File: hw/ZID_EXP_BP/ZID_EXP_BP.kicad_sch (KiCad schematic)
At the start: 47 parts, among them J1 FFC/FPC-40 Socket, J2 Conn_02x05_2.54mm, J3 Conn_02x05_2.54mm, J4 USB-C PWR ONLY, J6 Conn_02x03_Odd_Even, J7 Conn_02x03_Odd_Even, J9 HDR 2x10 Pin, Q1 DMG2305UX, U1 74HCT138

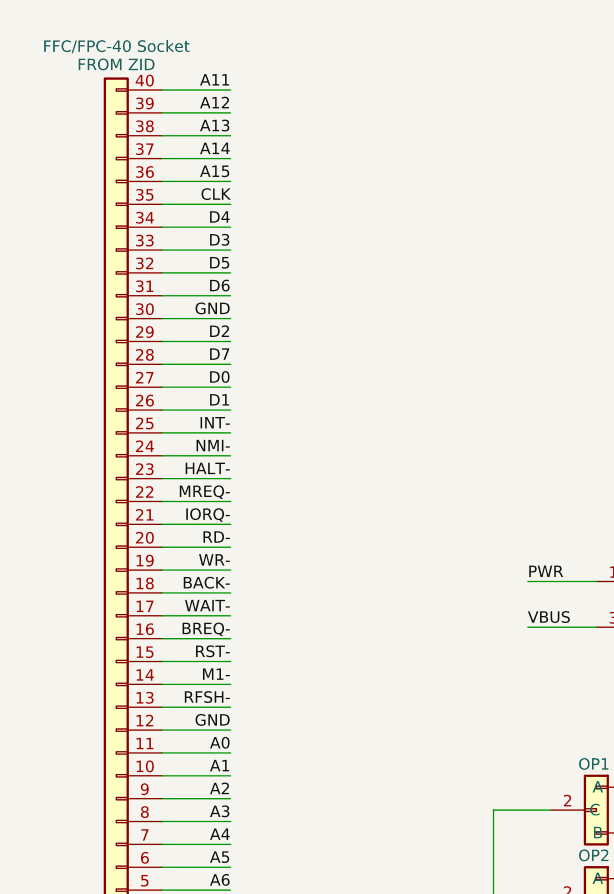
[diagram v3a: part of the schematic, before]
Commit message: 74FCT541 to 74FCT2245. Move GND around CLK on ZID-POD connector
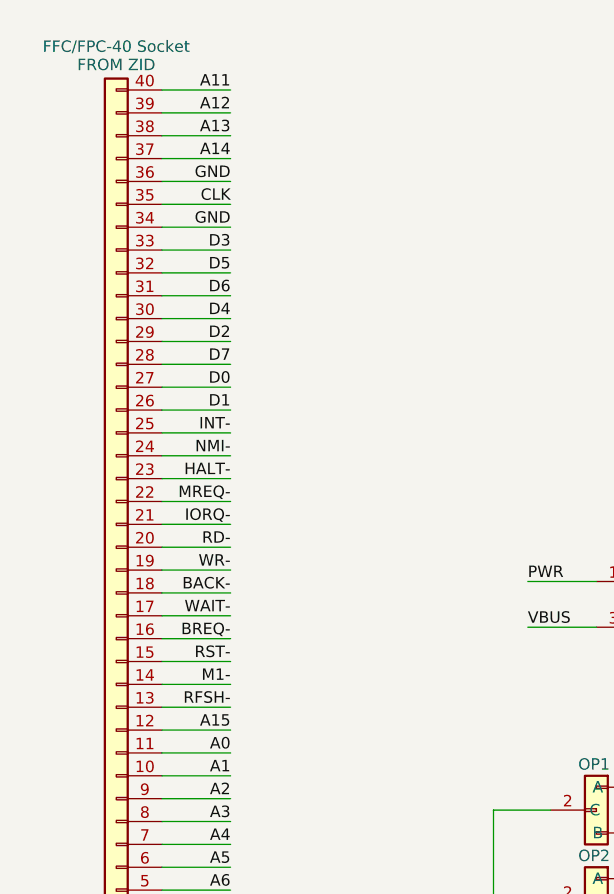
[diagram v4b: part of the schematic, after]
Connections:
- net A15: now also J1.12 (Pin_12); no longer J1.36 (Pin_36)
- net D4: now also J1.30 (Pin_30); no longer J1.34 (Pin_34)
- net GND: now also J1.34 (Pin_34), J1.36 (Pin_36); no longer J1.12 (Pin_12), J1.30 (Pin_30)
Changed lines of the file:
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@@
 	(title_block
 		(title "ZID EXPANSION BACKPLANE")
-		(date "2026-04-18")
+		(date "2026-04-21")
 		(rev "PR1.0")
 		(company "SilkyDESIGN")
@@
 		)
 	)
+	(label "GND"
+		(at 39.37 35.56 180)
+		(effects
+			(font
+				(size 1.27 1.27)
+			)
+			(justify right bottom)
+		)
+		(property "Note" "{not Z80 pin}"
+			(at 39.37 34.29 0)
+			(effects
+				(font
+					(size 1.27 1.27)
+					(italic yes)
+				)
+				(justify left)
+			)
+		)
+	)
 	(label "WAIT-"
 		(at 39.37 78.74 180)
@@
 		)
 	)
-	(label "A15"
-		(at 39.37 30.48 180)
-		(effects
-			(font
-				(size 1.27 1.27)
-			)
-			(justify right bottom)
-		)
-	)
 	(label "P45"
 		(at 152.4 41.91 0)
@@
 		)
 	)
+	(label "GND"
+		(at 39.37 30.48 180)
+		(effects
+			(font
+				(size 1.27 1.27)
+			)
+			(justify right bottom)
+		)
+		(property "Note" "{not Z80 pin}"
+			(at 39.37 29.21 0)
+			(effects
+				(font
+					(size 1.27 1.27)
+					(italic yes)
+				)
+				(justify left)
+			)
+		)
+	)
 	(label "P47"
 		(at 97.79 46.99 0)
@@
 		)
 	)
-	(label "GND"
-		(at 39.37 45.72 180)
-		(effects
-			(font
-				(size 1.27 1.27)
-			)
-			(justify right bottom)
-		)
-	)
 	(label "RFSH-"
 		(at 152.4 82.55 0)
@@
 		)
 	)
+	(label "D4"
+		(at 39.37 45.72 180)
+		(effects
+			(font
+				(size 1.27 1.27)
+			)
+			(justify right bottom)
+		)
+		(property "Note" "{not Z80 pin}"
+			(at 39.624 44.45 0)
+			(effects
+				(font
+					(size 1.27 1.27)
+					(italic yes)
+				)
+				(justify left)
+			)
+		)
+	)
 	(label "BACK-"
 		(at 39.37 76.2 180)
@@
 		)
 	)
-	(label "GND"
-		(at 39.37 91.44 180)
-		(effects
-			(font
-				(size 1.27 1.27)
-			)
-			(justify right bottom)
-		)
-	)
 	(label "MREQ-"
 		(at 39.37 66.04 180)
@@
 		)
 	)
-	(label "D4"
-		(at 39.37 35.56 180)
+	(label "A15"
+		(at 39.37 91.44 180)
 		(effects
 			(font
@@
 			(justify right bottom)
 		)
+		(property "Note" "{not Z80 pin}"
+			(at 39.624 90.424 0)
+			(effects
+				(font
+					(size 1.27 1.27)
+					(italic yes)
+				)
+				(justify left)
+			)
+		)
 	)
